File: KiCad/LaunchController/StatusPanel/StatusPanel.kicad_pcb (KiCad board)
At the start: 2 copper layers, 95 x 85 mm, 6 parts

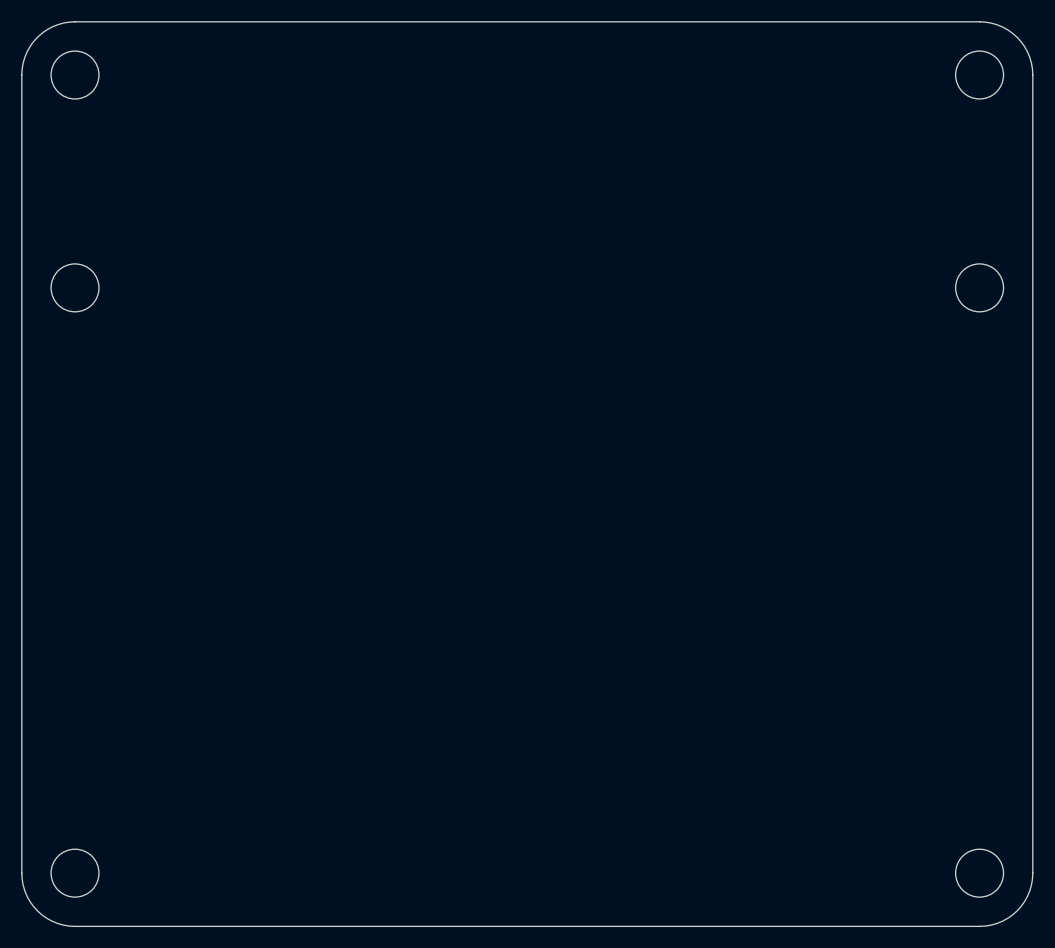
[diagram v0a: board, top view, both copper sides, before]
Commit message: LEDスイッチ類の取り付け穴を追加
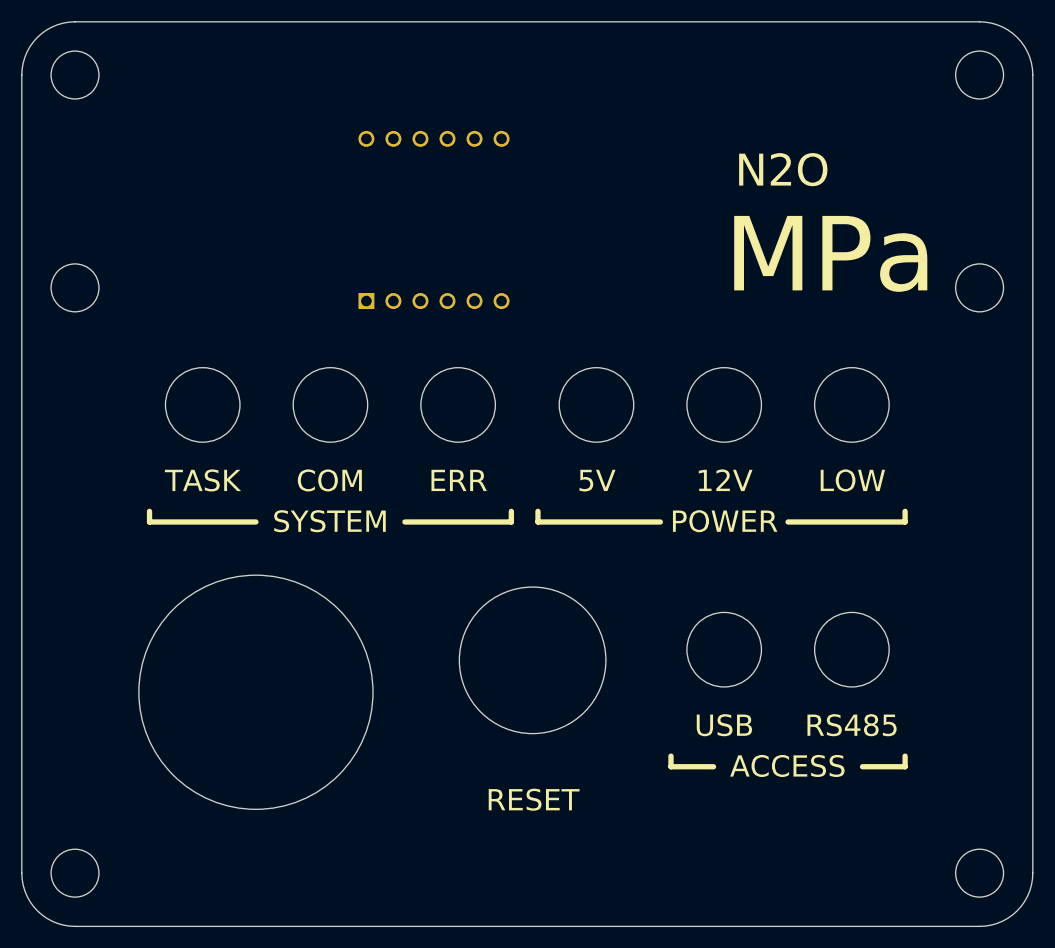
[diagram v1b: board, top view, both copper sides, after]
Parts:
- added REF**: MountingHole_6mm, MountingHole:MountingHole_6mm, F.Cu at (97.8, 80.9)
- added REF**: MountingHole_6mm, MountingHole:MountingHole_6mm, F.Cu at (110.8, 80.9)
- added REF**: MountingHole_6mm, MountingHole:MountingHole_6mm, F.Cu at (122.8, 103.9)
- added REF**: MountingHole_6mm, MountingHole:MountingHole_6mm, F.Cu at (104.8, 104.9)
- added REF**: MountingHole_6mm, MountingHole:MountingHole_6mm, F.Cu at (134.8, 103.9)
- added REF**: MountingHole_6mm, MountingHole:MountingHole_6mm, F.Cu at (134.8, 80.9)
- added REF**: MountingHole_6mm, MountingHole:MountingHole_6mm, F.Cu at (85.8, 80.9)
- added REF**: MountingHole_6mm, MountingHole:MountingHole_6mm, F.Cu at (122.8, 80.9)
- added REF**: MountingHole_6mm, MountingHole:MountingHole_6mm, F.Cu at (78.8, 107.9)
- added REF**: MountingHole_6mm, MountingHole:MountingHole_6mm, F.Cu at (73.8, 80.9)
- added U1: CC56-12EWA, Display_7Segment:CA56-12CGKWA, F.Cu at (89.2, 71.1)
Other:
- board text added: "12V"
- board text added: "5V"
- board text added: "ACCESS"
- board text added: "B"
- board text added: "COM"
- board text added: "ERR"
- board text added: "G"
- board text added: "LOW"
- board text added: "MPa"
- board text added: "N2O"
- board text added: "O"
- board text added: "POWER"
- board text added: "R"
- board text added: "RESET"
- board text added: "RS485"
- board text added: "SYSTEM"
- board text added: "TASK"
- board text added: "USB"
